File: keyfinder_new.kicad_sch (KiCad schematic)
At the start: 20 parts, among them U1 NRF52832, X1 32MHz, X2 32.768kHz

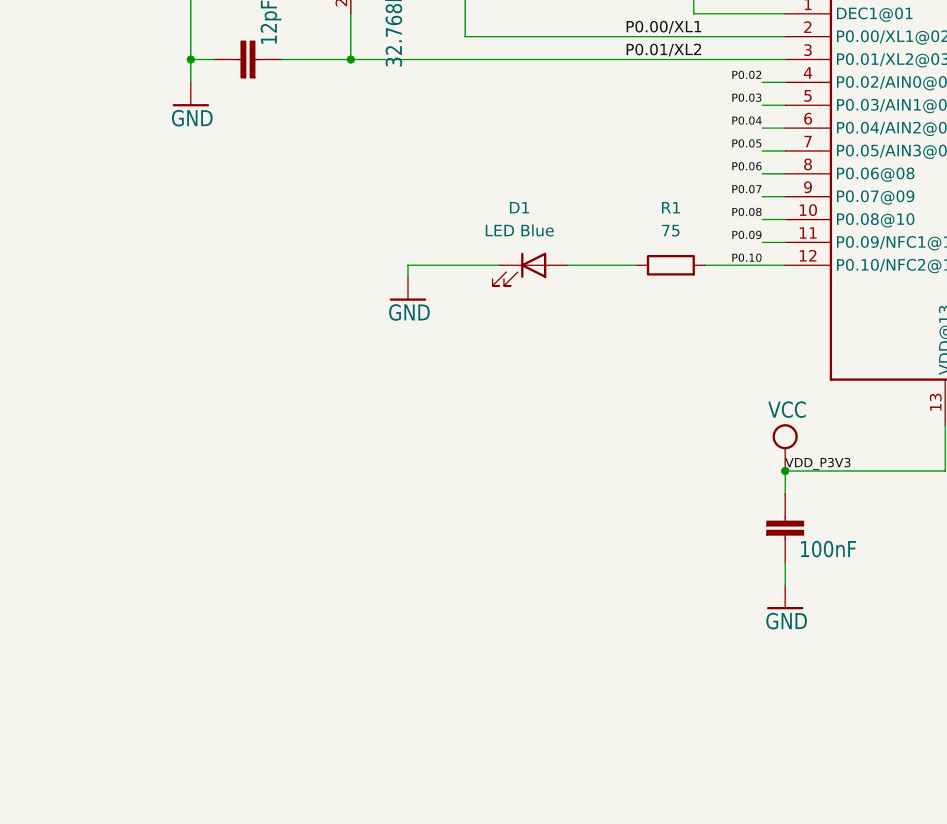
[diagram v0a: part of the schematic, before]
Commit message: Ajout de quelques composants sur le schema
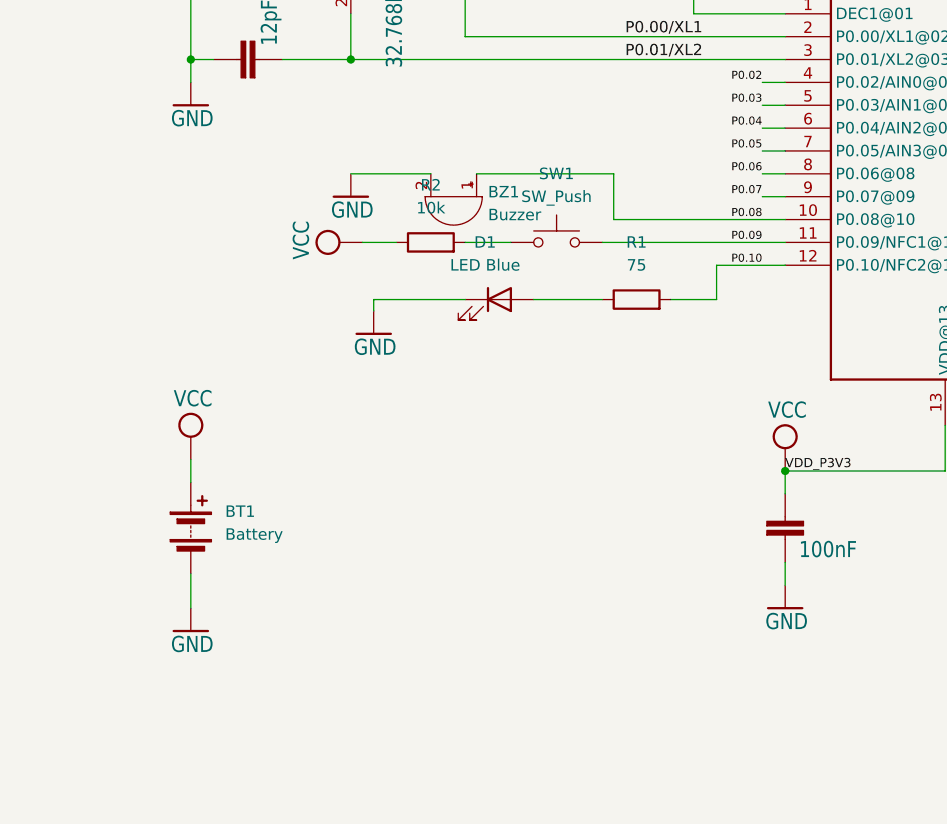
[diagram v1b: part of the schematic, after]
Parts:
- added BT1: Battery, Battery:BatteryHolder_Keystone_1060_1x2032, symbol Device:Battery
- added BZ1: Buzzer, Buzzer_Beeper:Buzzer_Murata_PKMCS0909E, symbol Device:Buzzer
- added R2: 10k, Resistor_SMD:R_0805_2012Metric, symbol Device:R
- added SW1: SW_Push, Button_Switch_THT:SW_CW_GPTS203211B, symbol Switch:SW_Push
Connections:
- net GND: now also BT1.2 (-), BZ1.2 (+)
- net P0.08: now also BZ1.1 (-)
- net P0.09: now also SW1.2
- net VCC: now also BT1.1 (+), R2.1
- new net: R2.2, SW1.1
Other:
- moved on the sheet: D1, R1

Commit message: Ajout des composants manquants et debut du routage sur le PCB
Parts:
- added J3: Conn_ARM_SWD_TagConnect_TC2030, Connector:Tag-Connect_TC2030-IDC-FP_2x03_P1.27mm_Vertical, symbol Connector:Conn_ARM_SWD_TagConnect_TC2030
- added R3: 10k, Resistor_SMD:R_0805_2012Metric, symbol Device:R
- added SW2: SW_Omron_B3FS, Button_Switch_SMD:SW_SPST_Omron_B3FS-100xP, symbol Switch:SW_Omron_B3FS
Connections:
- net GND: now also J3.5 (GND), SW2.1
- net P0.21/RESET: now also J3.3 (~{RESET}), R3.2, SW2.2
- net SWDCLK: now also J3.4 (SWCLK)
- net SWDIO: now also J3.2 (SWDIO)
- net VCC: now also J3.1 (VCC), R3.1

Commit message: Fin du routage
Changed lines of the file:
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@@
     (stroke (width 0.1524) (type solid))
+  )
+  (wire (pts (xy 132.08 161.29) (xy 132.08 162.56))
+    (stroke (width 0) (type default))
   )
   (wire (pts (xy 236.22 83.82) (xy 238.76 83.82))
@@
   (label "DEC1" (at 86.36 60.96 0) (fields_autoplaced)
     (effects (font (size 1.2446 1.2446)) (justify left bottom))
+  )
+  (label "VDD_P3V3" (at 57.15 121.92 0) (fields_autoplaced)
+    (effects (font (size 1.016 1.016)) (justify left bottom))
   )
   (label "P0.00/XL1" (at 88.9 99.06 0) (fields_autoplaced)
@@
     )
   )
-  (symbol (lib_id "keyfinder_new-eagle-import:VCC") (at 132.08 160.02 0) (unit 1)
-    (in_bom yes) (on_board yes) (dnp no)
-    (property "Reference" "#VDD_NRF06" (at 132.08 160.02 0)
-      (effects (font (size 1.27 1.27)) hide)
-    )
-    (property "Value" "VCC" (at 130.175 156.845 0)
-      (effects (font (size 1.778 1.5113)) (justify left bottom))
-    )
-    (property "Footprint" "" (at 132.08 160.02 0)
-      (effects (font (size 1.27 1.27)) hide)
-    )
-    (property "Datasheet" "" (at 132.08 160.02 0)
-      (effects (font (size 1.27 1.27)) hide)
-    )
+  (symbol (lib_id "keyfinder_new-eagle-import:VCC") (at 132.08 158.75 0) (unit 1)
+    (in_bom yes) (on_board yes) (dnp no)
+    (property "Reference" "#VDD_NRF06" (at 132.08 158.75 0)
+      (effects (font (size 1.27 1.27)) hide)
+    )
+    (property "Value" "VCC" (at 130.175 155.575 0)
+      (effects (font (size 1.778 1.5113)) (justify left bottom))
+    )
+    (property "Footprint" "" (at 132.08 158.75 0)
+      (effects (font (size 1.27 1.27)) hide)
+    )
+    (property "Datasheet" "" (at 132.08 158.75 0)
+      (effects (font (size 1.27 1.27)) hide)
+    )

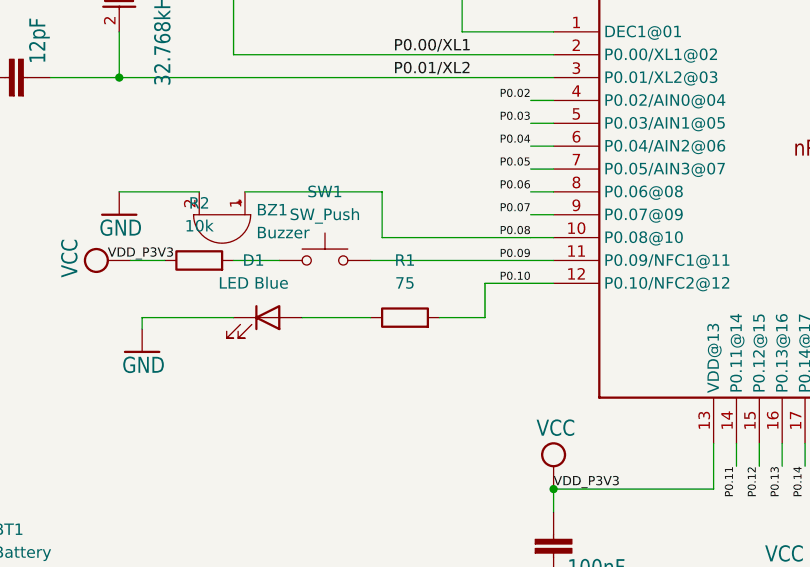
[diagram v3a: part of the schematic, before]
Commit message: ajout des references et liens vers DigiKey dans les composants sur le schematic
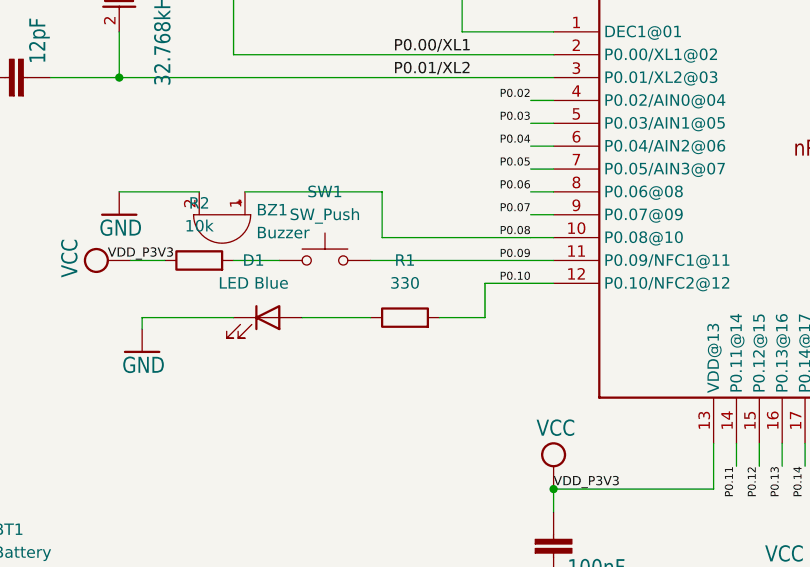
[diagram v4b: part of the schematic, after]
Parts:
- BT1: Link (none) -> https://www.digikey.fr/fr/products/detail/keystone-electron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; Ref (none) -> Keystone 1060
- BZ1: Link (none) -> https://www.digikey.fr/fr/products/detail/murata-electronic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; Ref (none) -> PKMCS0909E4000-R1
- D1: Link (none) -> https://www.digikey.fr/fr/products/detail/liteon/LTST-C171T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; Ref (none) -> LTST-C171TBKT
- J3: Link (none) -> https://www.digikey.fr/fr/products/detail/tag-connect-llc/T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; Ref (none) -> TC2030-IDC
- R1: value 75 -> 330; Link (none) -> https://www.digikey.fr/fr/products/detail/stackpole-electro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; Ref (none) -> RMCF0805JT330R
- R2, R3: Link (none) -> https://www.digikey.fr/fr/products/detail/stackpole-electro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; Ref (none) -> RMCF0805JT10K0
- SW1: Link (none) -> https://www.digikey.fr/fr/products/detail/cw-industries/GPT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; Ref (none) -> GPTS203211B
- SW2: Link (none) -> https://www.digikey.fr/fr/products/detail/omron-electronics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; Ref (none) -> B3FS-1002P
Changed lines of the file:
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@@
+      (effects (font (size 1.27 1.27)) hide)
+    )
+    (property "Ref" "Keystone 1060" (at 40.64 153.67 0)
+      (effects (font (size 1.27 1.27)) hide)
+    )
+    (property "Link" "https://www.digikey.fr/fr/products/detail/keystone-electronics/1060/303556" (at 40.64 153.67 0)
       (effects (font (size 1.27 1.27)) hide)
     )
@@
       (effects (font (size 1.27 1.27)) hide)
     )
+    (property "Ref" "RMCF0805JT10K0" (at 132.08 166.37 0)
+      (effects (font (size 1.27 1.27)) hide)
+    )
+    (property "Link" "https://www.digikey.fr/fr/products/detail/stackpole-electronics-inc/RMCF0805JT10K0/1757762" (at 132.08 166.37 0)
+      (effects (font (size 1.27 1.27)) hide)
+    )
     (pin "1")
     (pin "2")
@@
       (effects (font (size 1.27 1.27)) hide)
     )
+    (property "Ref" "LTST-C171TBKT" (at 74.93 128.27 0)
+      (effects (font (size 1.27 1.27)) hide)
+    )
+    (property "Link" "https://www.digikey.fr/fr/products/detail/liteon/LTST-C171TBKT/388528" (at 74.93 128.27 0)
+      (effects (font (size 1.27 1.27)) hide)
+    )
     (pin "1")
     (pin "2")
@@
     )
     (property "Datasheet" "https://www.tag-connect.com/wp-content/uploads/bsk-pdf-manager/TC2030-CTX_1.pdf" (at 199.39 132.08 0)
+      (effects (font (size 1.27 1.27)) hide)
+    )
+    (property "Ref" "TC2030-IDC" (at 199.39 147.32 0)
+      (effects (font (size 1.27 1.27)) hide)
+    )
+    (property "Link" "https://www.digikey.fr/fr/products/detail/tag-connect-llc/TC2030-IDC/4571121" (at 199.39 147.32 0)
       (effects (font (size 1.27 1.27)) hide)
     )
@@
       (effects (font (size 1.27 1.27)) hide)
     )
+    (property "Ref" "B3FS-1002P" (at 124.46 171.45 0)
+      (effects (font (size 1.27 1.27)) hide)
+    )
+    (property "Link" "https://www.digikey.fr/fr/products/detail/omron-electronics-inc-emc-div/B3FS-1002P/277815" (at 124.46 171.45 0)
+      (effects (font (size 1.27 1.27)) hide)
+    )
     (pin "2")
     (pin "1")
@@
       (effects (font (size 1.27 1.27)) hide)
     )
+    (property "Ref" "PKMCS0909E4000-R1" (at 69.85 116.84 90)
+      (effects (font (size 1.27 1.27)) hide)
+    )
+    (property "Link" "https://www.digikey.fr/fr/products/detail/murata-electronics/PKMCS0909E4000-R1/4878400" (at 69.85 116.84 90)
+      (effects (font (size 1.27 1.27)) hide)
+    )
     (pin "1")
     (pin "2")
@@
       (effects (font (size 1.27 1.27)))
     )
-    (property "Value" "75" (at 90.17 124.46 90)
+    (property "Value" "330" (at 90.17 124.46 90)
       (effects (font (size 1.27 1.27)))
     )
@@
     )
     (property "Datasheet" "~" (at 90.17 128.27 0)
+      (effects (font (size 1.27 1.27)) hide)
+    )
+    (property "Ref" "RMCF0805JT330R" (at 90.17 128.27 90)
+      (effects (font (size 1.27 1.27)) hide)
+    )
+    (property "Link" "https://www.digikey.fr/fr/products/detail/stackpole-electronics-inc/RMCF0805JT330R/1757830" (at 90.17 128.27 90)
       (effects (font (size 1.27 1.27)) hide)
     )
@@
       (effects (font (size 1.27 1.27)) hide)
     )
+    (property "Ref" "GPTS203211B" (at 81.28 121.92 0)
+      (effects (font (size 1.27 1.27)) hide)
+    )
+    (property "Link" "https://www.digikey.fr/fr/products/detail/cw-industries/GPTS203211B/3190590?s=N4IgTCBcDaIOIAUAqBlMAGAzGAjDgQiALoC%2BQA" (at 81.28 121.92 0)
+      (effects (font (size 1.27 1.27)) hide)
+    )
     (pin "1")
     (pin "2")
@@
       (effects (font (size 1.27 1.27)) hide)
     )
+    (property "Ref" "RMCF0805JT10K0" (at 67.31 121.92 90)
+      (effects (font (size 1.27 1.27)) hide)
+    )
+    (property "Link" "https://www.digikey.fr/fr/products/detail/stackpole-electronics-inc/RMCF0805JT10K0/1757762" (at 67.31 121.92 90)
+      (effects (font (size 1.27 1.27)) hide)
+    )

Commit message: Passage sur le vrai PCB
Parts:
- J3: footprint Connector:Tag-Connect_TC2030-IDC-FP_2x03_P1.27mm_Vertical -> Connector:Tag-Connect_TC2030-IDC-NL_2x03_P1.27mm_Vertical
- SW1: footprint Button_Switch_THT:SW_CW_GPTS203211B -> Button_Switch_SMD:SW_SPST_PTS810
- SW2: footprint Button_Switch_SMD:SW_SPST_Omron_B3FS-100xP -> Button_Switch_SMD:SW_SPST_PTS810
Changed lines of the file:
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@@
       (effects (font (size 1.27 1.27)) (justify right))
     )
-    (property "Footprint" "Connector:Tag-Connect_TC2030-IDC-FP_2x03_P1.27mm_Vertical" (at 199.39 129.54 0)
+    (property "Footprint" "Connector:Tag-Connect_TC2030-IDC-NL_2x03_P1.27mm_Vertical" (at 199.39 129.54 0)
       (effects (font (size 1.27 1.27)) hide)
     )
@@
       (effects (font (size 1.27 1.27)) hide)
     )
+    (pin "1")
     (pin "2")
     (pin "3")
+    (pin "4")
+    (pin "5")
     (pin "6")
-    (pin "5")
-    (pin "4")
-    (pin "1")
     (instances
       (project "keyfinder_new"
@@
       (effects (font (size 1.27 1.27)))
     )
-    (property "Footprint" "Button_Switch_SMD:SW_SPST_Omron_B3FS-100xP" (at 124.46 166.37 0)
+    (property "Footprint" "Button_Switch_SMD:SW_SPST_PTS810" (at 124.46 166.37 0)
       (effects (font (size 1.27 1.27)) hide)
     )
@@
       (effects (font (size 1.27 1.27)) hide)
     )
-    (pin "2")
-    (pin "1")
+    (pin "1")
+    (pin "2")
     (instances
       (project "keyfinder_new"
@@
       (effects (font (size 1.27 1.27)))
     )
-    (property "Footprint" "Button_Switch_THT:SW_CW_GPTS203211B" (at 81.28 116.84 0)
-      (effects (font (size 1.27 1.27)) hide)
-    )
+    (property "Footprint" "Button_Switch_SMD:SW_SPST_PTS810" (at 81.28 116.84 0)
+      (effects (font (size 1.27 1.27)) hide)
+    )

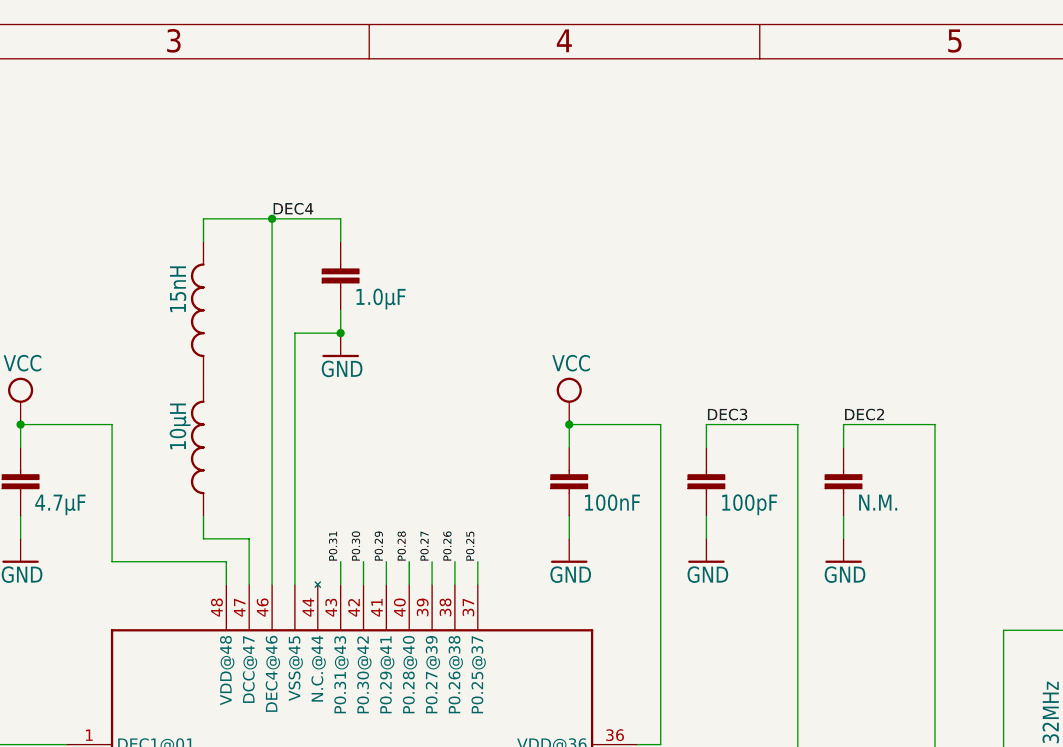
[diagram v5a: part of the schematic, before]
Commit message: Ajout du capteur de temperature au schema et au PCB et routage
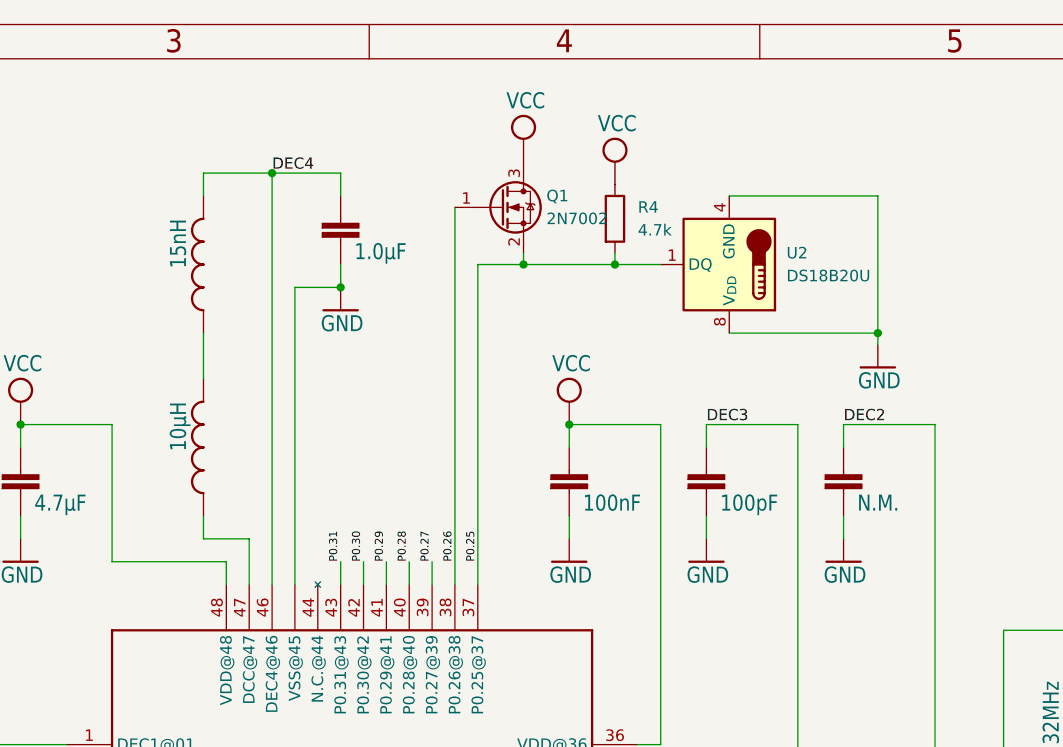
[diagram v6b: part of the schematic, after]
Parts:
- added Q1: 2N7002, Package_TO_SOT_SMD:SOT-23, symbol Transistor_FET:2N7002
- added R4: 4.7k, Resistor_SMD:R_0805_2012Metric, symbol Device:R
- added U2: DS18B20U, Package_SO:MSOP-8_3x3mm_P0.65mm, symbol Sensor_Temperature:DS18B20U
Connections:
- net GND: now also U2.4 (GND), U2.8 (V_{DD})
- net P0.25: now also Q1.2 (S), R4.2, U2.1 (DQ)
- net P0.26: now also Q1.1 (G)
- net VCC: now also Q1.3 (D), R4.1
